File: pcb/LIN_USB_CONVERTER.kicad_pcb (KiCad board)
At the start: 2 copper layers, 17.8 x 34 mm, 32 parts, among them J1 Conn_01x03, J2 Conn_01x03, J3 GS2, J4 USB_A, J5 Conn_01x02, P2 CONN_01X05, U1 TJA1028, U2 MAX12931, U3 MCP1700T-3302E/TT, U4 STM32F042G4U6

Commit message: Kicad update
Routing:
- net -BATT: track 62.3 -> 62.7 mm, vias 2 -> 3
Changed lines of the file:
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@@
-(kicad_pcb (version 4) (host pcbnew 4.0.7)
+(kicad_pcb (version 20171130) (host pcbnew "(2018-02-16 revision c95340fba)-makepkg")
   (general
-    (links 84)
-    (no_connects 7)
-    (area 140.121999 78.203999 158.102001 112.440001)
     (thickness 1.6)
     (drawings 20)
-    (tracks 272)
+    (tracks 276)
     (zones 0)
     (modules 32)
@@
       (layerselection 0x3ffff_80000001)
       (usegerberextensions true)
+      (usegerberattributes false)
+      (usegerberadvancedattributes false)
+      (creategerberjobfile false)
       (excludeedgelayer true)
       (linewidth 0.100000)
@@
       (hpglpenspeed 20)
       (hpglpendiameter 15)
-      (hpglpenoverlay 2)
       (psnegative false)
       (psa4output false)
@@
     (tags "capacitor 0402")
     (attr smd)
-    (fp_text reference C8 (at 1.5 0 540) (layer F.SilkS)
+    (fp_text reference C8 (at 1.5 0 180) (layer F.SilkS)
       (effects (font (size 0.4 0.4) (thickness 0.09)))
     )
@@
     (tags "capacitor 0402")
     (attr smd)
-    (fp_text reference C3 (at 1.524 0 540) (layer F.SilkS)
+    (fp_text reference C3 (at 1.524 0 180) (layer F.SilkS)
       (effects (font (size 0.4 0.4) (thickness 0.09)))
     )
@@
     (tags "capacitor 0603")
     (attr smd)
-    (fp_text reference C2 (at 1.778 0 360) (layer F.SilkS)
+    (fp_text reference C2 (at 1.778 0) (layer F.SilkS)
       (effects (font (size 0.4 0.4) (thickness 0.09)))
     )
@@
     (tags "capacitor 0402")
     (attr smd)
-    (fp_text reference C6 (at -1.524 0 450) (layer F.SilkS)
+    (fp_text reference C6 (at -1.524 0 90) (layer F.SilkS)
       (effects (font (size 0.4 0.4) (thickness 0.09)))
     )
@@
     (descr "Through hole straight pin header, 1x03, 2.54mm pitch, single row")
     (tags "Through hole pin header THT 1x03 2.54mm single row")
-    (fp_text reference J1 (at 1.27 1.524 450) (layer B.SilkS)
+    (fp_text reference J1 (at 1.27 1.524 90) (layer B.SilkS)
       (effects (font (size 0.4 0.4) (thickness 0.09)) (justify mirror))
     )
@@
     (fp_line (start 1.8 -6.85) (end 1.8 1.8) (layer B.CrtYd) (width 0.05))
     (fp_line (start 1.8 1.8) (end -1.8 1.8) (layer B.CrtYd) (width 0.05))
-    (fp_text user %R (at 0 -2.54 540) (layer B.Fab)
+    (fp_text user %R (at 0 -2.54 180) (layer B.Fab)
       (effects (font (size 0.4 0.4) (thickness 0.09)) (justify mirror))
     )
@@
     (fp_line (start 1.8 -4.35) (end 1.8 1.8) (layer B.CrtYd) (width 0.05))
     (fp_line (start 1.8 1.8) (end -1.8 1.8) (layer B.CrtYd) (width 0.05))
-    (fp_text user %R (at 0 -1.27 450) (layer B.Fab)
+    (fp_text user %R (at 0 -1.27 90) (layer B.Fab)
       (effects (font (size 0.4 0.4) (thickness 0.09)) (justify mirror))
     )
@@
     (pad "" np_thru_hole circle (at 5.842 -2.413) (size 1.5 1.5) (drill 1.5) (layers *.Cu *.Mask))
     (model Connect.3dshapes/USB_A.wrl
-      (at (xyz 0.14 0 0))
+      (offset (xyz 3.555999946594238 0 0))
       (scale (xyz 1 1 1))
       (rotate (xyz 0 0 90))
@@
   (segment (start 156.462 86.324) (end 155.554 85.416) (width 0.25) (layer F.Cu) (net 8))
   (segment (start 155.554 85.416) (end 155.504 85.416) (width 0.25) (layer F.Cu) (net 8))
+  (segment (start 151.143002 95.83) (end 150.382 95.83) (width 0.25) (layer F.Cu) (net 9))
+  (segment (start 151.905002 96.592) (end 151.143002 95.83) (width 0.25) (layer F.Cu) (net 9))
+  (segment (start 150.382 95.83) (end 149.227978 96.984022) (width 0.25) (layer F.Cu) (net 9))
+  (segment (start 149.227978 96.984022) (end 149.227978 98.484022) (width 0.25) (layer F.Cu) (net 9))
+  (segment (start 149.227978 98.484022) (end 147.588 100.124) (width 0.25) (layer F.Cu) (net 9))
+  (segment (start 147.588 100.124) (end 147.588 100.87) (width 0.25) (layer F.Cu) (net 9))
+  (segment (start 151.905002 96.338998) (end 152.16 96.084) (width 0.25) (layer F.Cu) (net 9))
+  (via (at 152.16 96.084) (size 0.6) (drill 0.4) (layers F.Cu B.Cu) (net 9))
+  (segment (start 152.525002 97.212) (end 151.905002 96.592) (width 0.25) (layer F.Cu) (net 9))
+  (segment (start 151.905002 96.592) (end 151.905002 96.338998) (width 0.25) (layer F.Cu) (net 9))
   (segment (start 154.192 97.212) (end 153.56 97.212) (width 0.25) (layer F.Cu) (net 9))
-  (segment (start 147.588 100.124) (end 147.588 100.87) (width 0.25) (layer F.Cu) (net 9))
-  (segment (start 152.525002 97.212) (end 151.143002 95.83) (width 0.25) (layer F.Cu) (net 9))
-  (segment (start 149.227978 98.484022) (end 147.588 100.124) (width 0.25) (layer F.Cu) (net 9))
-  (segment (start 151.143002 95.83) (end 149.874 95.83) (width 0.25) (layer F.Cu) (net 9))
   (segment (start 154.192 97.212) (end 152.525002 97.212) (width 0.25) (layer F.Cu) (net 9))
-  (segment (start 149.874 95.83) (end 149.227978 96.476022) (width 0.25) (layer F.Cu) (net 9))
-  (segment (start 149.227978 96.476022) (end 149.227978 98.484022) (width 0.25) (layer F.Cu) (net 9))
   (segment (start 150.128 106.244) (end 150.128 109.292) (width 0.25) (layer F.Cu) (net 9))
   (segment (start 150.128 109.292) (end 150.382 109.546) (width 0.25) (layer F.Cu) (net 9))
@@
     (polygon
       (pts
-        (xy 140.222 97.1) (xy 149.366 97.1) (xy 149.366 94.306) (xy 154.192 94.306) (xy 154.192 91.258)
+        (xy 140.222 97.1) (xy 148.096 97.1) (xy 148.096 94.56) (xy 154.192 94.56) (xy 154.192 91.258)
         (xy 157.748 91.258) (xy 158.002 91.258) (xy 158.002 78.304) (xy 140.222 78.304)
       )
@@
     (polygon
       (pts
-        (xy 140.222 97.1) (xy 149.366 97.1) (xy 149.366 94.306) (xy 154.192 94.306) (xy 154.192 91.258)
+        (xy 140.222 97.1) (xy 148.096 97.1) (xy 148.096 94.56) (xy 154.192 94.56) (xy 154.192 91.258)
         (xy 157.748 91.258) (xy 158.002 91.258) (xy 158.002 78.304) (xy 140.222 78.304)
       )

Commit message: frame reception fixes
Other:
- board text removed: "+BAT"
- board text removed: "-BAT"
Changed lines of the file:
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@@
     (aux_axis_origin 154.7 109.8)
     (grid_origin 154.7 109.8)
-    (visible_elements 7FFEDF7F)
+    (visible_elements 7FFFDF7F)
     (pcbplotparams
       (layerselection 0x3ffff_80000001)
@@
     (effects (font (size 0.6 0.6) (thickness 0.1)) (justify mirror))
   )
-  (gr_text -BAT (at 153.43 99.64) (layer B.SilkS)
+  (gr_text BAT- (at 153.43 99.64) (layer B.SilkS)
     (effects (font (size 0.6 0.6) (thickness 0.1)) (justify mirror))
   )
-  (gr_text +BAT (at 150.89 99.64) (layer B.SilkS)
+  (gr_text BAT+ (at 150.89 99.64) (layer B.SilkS)
     (effects (font (size 0.6 0.6) (thickness 0.1)) (justify mirror))
   )
@@
   (gr_line (start 140.222 78.304) (end 158.002 78.304) (layer Edge.Cuts) (width 0.2))
   (gr_line (start 140.222 112.304) (end 140.222 78.304) (layer Edge.Cuts) (width 0.2))
-  (gr_text GND (at 141.746 85.162 180) (layer F.SilkS)
+  (gr_text GND (at 141.492 82.622 180) (layer F.SilkS)
     (effects (font (size 0.6 0.6) (thickness 0.1)))
   )
-  (gr_text RST (at 143.524 93.798 90) (layer F.SilkS)
+  (gr_text RST (at 141.492 92.782) (layer F.SilkS)
     (effects (font (size 0.6 0.6) (thickness 0.1)))
   )
-  (gr_text DIO (at 141.746 87.702 180) (layer F.SilkS)
+  (gr_text DIO (at 141.492 85.162 180) (layer F.SilkS)
     (effects (font (size 0.6 0.6) (thickness 0.1)))
   )
-  (gr_text 3V3 (at 141.746 90.242) (layer F.SilkS)
+  (gr_text CLK (at 141.492 87.702) (layer F.SilkS)
     (effects (font (size 0.6 0.6) (thickness 0.1)))
   )
-  (gr_text CLK (at 141.746 92.782) (layer F.SilkS)
+  (gr_text 3V3 (at 141.492 90.242) (layer F.SilkS)
     (effects (font (size 0.6 0.6) (thickness 0.1)))
   )

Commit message: Naming update
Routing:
- net GND: track 36.0 -> 38.7 mm, vias 3 -> 4
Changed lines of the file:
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@@
     (thickness 1.6)
     (drawings 20)
-    (tracks 276)
+    (tracks 280)
     (zones 0)
     (modules 32)
@@
   )
   (gr_line (start 155.867134 85.010166) (end 153.221534 85.010166) (angle 90) (layer B.SilkS) (width 0.2))
+  (segment (start 152.668 88.718) (end 152.16 88.718) (width 0.25) (layer F.Cu) (net 1))
+  (segment (start 153.618 87.768) (end 152.668 88.718) (width 0.25) (layer F.Cu) (net 1))
+  (via (at 152.16 88.718) (size 0.6) (drill 0.4) (layers F.Cu B.Cu) (net 1))
+  (segment (start 154.462 87.768) (end 153.618 87.768) (width 0.25) (layer F.Cu) (net 1))
   (segment (start 152.668 86.474) (end 152.168 86.474) (width 0.25) (layer F.Cu) (net 1))
   (segment (start 152.168 86.474) (end 150.983 85.289) (width 0.25) (layer F.Cu) (net 1))
@@
   (segment (start 141.746 94.052) (end 142.146 94.052) (width 0.25) (layer F.Cu) (net 7))
   (segment (start 148.482 89.864) (end 148.482 90.389) (width 0.25) (layer F.Cu) (net 7))
+  (segment (start 152.41486 82.87812) (end 153.165429 83.628689) (width 0.25) (layer F.Cu) (net 8))
   (segment (start 155.504 85.416) (end 155.504 84.916) (width 0.25) (layer F.Cu) (net 8))
   (segment (start 155.504 84.916) (end 154.216689 83.628689) (width 0.25) (layer F.Cu) (net 8))
   (segment (start 154.216689 83.628689) (end 153.165429 83.628689) (width 0.25) (layer F.Cu) (net 8))
-  (segment (start 153.165429 83.628689) (end 152.41486 82.87812) (width 0.25) (layer F.Cu) (net 8))
   (segment (start 156.462 88.718) (end 156.462 86.324) (width 0.25) (layer F.Cu) (net 8))
   (segment (start 156.462 86.324) (end 155.554 85.416) (width 0.25) (layer F.Cu) (net 8))

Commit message: PCB release
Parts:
- added C7: 10u, Capacitors_SMD:C_0402, F.Cu at (156.5, 98.4)
- J2: value Conn_01x03 -> TerminalBlock
- U1: value TJA1028 -> TJA1028TK/3V3/20/J
- U2: value MAX12931 -> MAX12931BASA+
- moved C3 0.28 mm to (155.2, 98.4)
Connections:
- U1 pad 7: Net-(U1-Pad7) -> (no net)
- U4 pad 10: Net-(U4-Pad10) -> (no net)
- U4 pad 11: Net-(U4-Pad11) -> (no net)
- U4 pad 12: Net-(U4-Pad12) -> (no net)
- U4 pad 13: Net-(U4-Pad13) -> (no net)
- U4 pad 2: Net-(U4-Pad2) -> (no net)
- U4 pad 23: Net-(U4-Pad23) -> (no net)
- U4 pad 24: Net-(U4-Pad24) -> (no net)
- U4 pad 25: Net-(U4-Pad25) -> (no net)
- U4 pad 26: Net-(U4-Pad26) -> (no net)
- U4 pad 3: Net-(U4-Pad3) -> (no net)
- U4 pad 6: Net-(U4-Pad6) -> (no net)
- U4 pad 9: Net-(U4-Pad9) -> (no net)
- mh1 pad 1: (no net) -> -BATT
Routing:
- net Net-(C1-Pad1): track 26.1 -> 28.3 mm
- net -BATT: track 62.7 -> 64.2 mm
- net +3.3VA: track 22.4 -> 23.7 mm
- net Net-(J3-Pad2): track 9.81 -> 10.5 mm
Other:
- board text added: "MASTER RESISTOR"

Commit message: PCB release
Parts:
- C7: footprint Capacitors_SMD:C_0402 -> Capacitors_SMD:C_0603
- moved C7 0.23 mm to (156.4, 98.6)
- moved C3 0.13 mm to (155.1, 98.4)
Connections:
- D1 pad 1: Net-(D1-Pad1) -> +BATT
- D1 pad 2: +BATT -> Net-(D1-Pad2)
- D3 pad 1: +BATT -> Net-(D3-Pad1)
- D3 pad 2: Net-(D3-Pad2) -> +BATT
- J1 pad 1: +BATT -> Net-(D1-Pad2)
- J2 pad 3: +BATT -> Net-(D1-Pad2)
- R1 pad 2: Net-(D3-Pad2) -> Net-(D3-Pad1)
- R2 pad 2: Net-(D1-Pad1) -> +BATT
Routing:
- net Net-(D1-Pad2): track 0.00 -> 18.4 mm
- net Net-(D3-Pad1): track 0.00 -> 4.56 mm
- net Net-(D1-Pad1): track 4.55 -> 0.00 mm
- net Net-(D3-Pad2): track 2.09 -> 0.00 mm
- net -BATT: track 64.2 -> 62.1 mm
- net +BATT: track 20.0 -> 18.3 mm

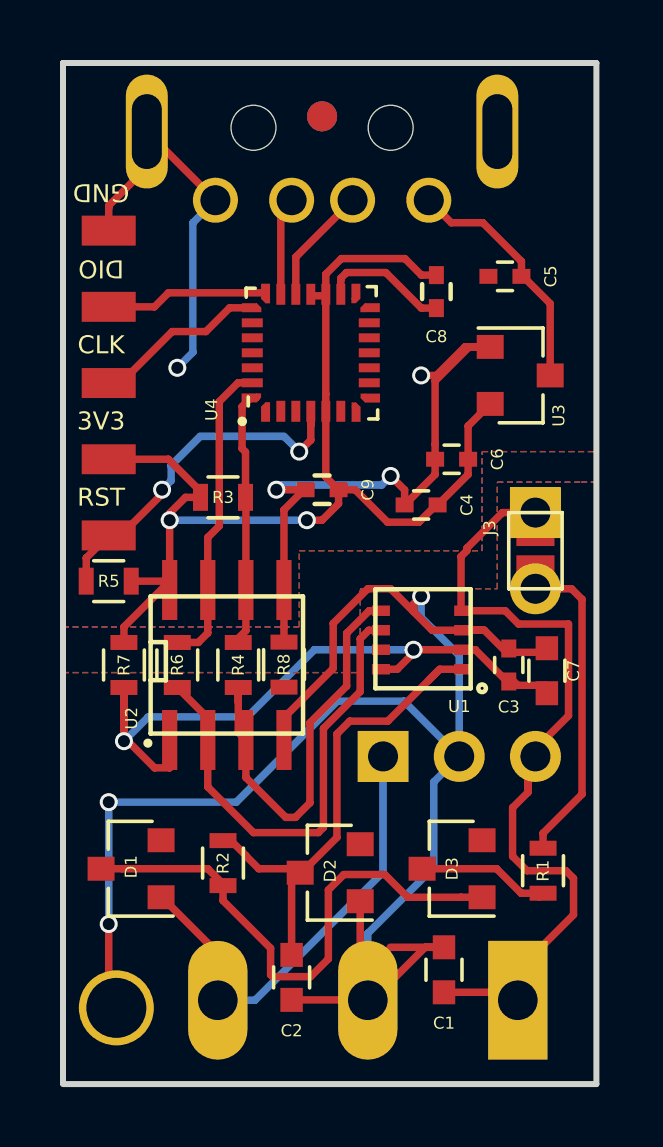
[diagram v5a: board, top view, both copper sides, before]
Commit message: Remove of galvanic spearator
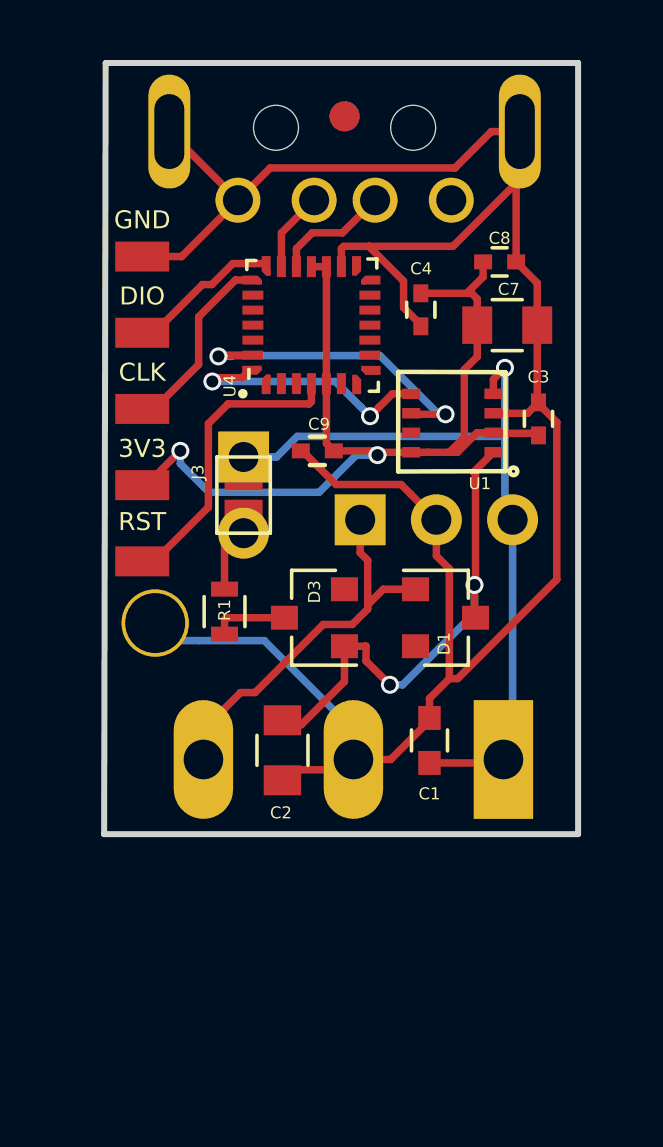
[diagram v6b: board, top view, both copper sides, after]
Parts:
- removed C5, C6: 100n, Capacitors_SMD:C_0402
- removed D2: 1N5819HW-7-F, Diodes_SMD:D_SOT-23_ANK
- removed R2: 50, Resistors_SMD:R_0603
- removed R3, R5: 10k, Resistors_SMD:R_0603
- removed R4, R6, R7, R8: 0, Resistors_SMD:R_0603
- removed U2: MAX12931BASA+, usb_ccb_custom:SOIC-8-N_MAXIM
- removed U3: MCP1700T-3302E/TT, TO_SOT_Packages_SMD:SOT-23
- C2: footprint Capacitors_SMD:C_0603 -> Capacitors_SMD:C_0805
- C7: value 10u -> 4,7u; footprint Capacitors_SMD:C_0603 -> Capacitors_SMD:C_0805
- U1: footprint usb_ccb_custom:HVSON8 -> ucan_custom:HVSON8
- moved R1 13.7 mm to (145.6, 96.6)
- moved D1 13.4 mm to (153.0, 96.8), turned to 0 degrees
- moved mh1 12.9 mm to (143.3, 97.0)
- moved C7 11.6 mm to (155.0, 87.0), turned to 180 degrees
- moved J3 9.90 mm to (146.2, 92.7)
- moved J5 9.90 mm to (146.2, 91.4)
- moved D3 9.54 mm to (148.6, 96.8)
- moved C3 8.26 mm to (156.1, 90.2)
- moved J2 8.04 mm to (154.9, 101.5)
- moved J1 7.92 mm to (150.1, 93.5)
- moved C1 7.66 mm to (152.4, 100.9)
- moved C2 7.58 mm to (147.5, 101.2)
- moved U1 7.30 mm to (151.9, 91.3)
- moved C4 6.51 mm to (152.1, 86.5), turned to 270 degrees
- moved C8 2.33 mm to (154.8, 84.9), turned to 0 degrees
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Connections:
- C2 pad 1: Net-(C2-Pad1) -> +BATT
- C4 pad 1: +3V3 -> +3.3VA
- C4 pad 2: GND -> -BATT
- C8 pad 1: +3V3 -> +3.3VA
- C8 pad 2: GND -> -BATT
- C9 pad 1: +3V3 -> +3.3VA
- C9 pad 2: GND -> -BATT
- J4 pad 1: +5V -> (no net)
- J4 pad 4: GND -> -BATT
- J4 pad 5: GND -> -BATT
- P2 pad 1: GND -> -BATT
- P2 pad 4: +3V3 -> +3.3VA
- U1 pad 1: Net-(C2-Pad1) -> +BATT
- U1 pad 5: Net-(R4-Pad1) -> USART_RX
- U1 pad 6: Net-(R6-Pad1) -> USART_TX
- U4 pad 16: GND -> -BATT
- U4 pad 17: +3V3 -> +3.3VA
- U4 pad 18: +3V3 -> +3.3VA
- U4 pad 27: /USART_TX -> USART_TX
- U4 pad 28: /USART_RX -> USART_RX
- U4 pad 5: +3V3 -> +3.3VA
- mh1 pad 1: -BATT -> (no net)
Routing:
- net GND: track 38.7 -> 0.00 mm, vias 4 -> 0
- net +3V3: track 38.2 -> 0.00 mm, vias 2 -> 0
- net -BATT: track 62.1 -> 79.3 mm, vias 3 -> 0
- net Net-(C2-Pad1): track 16.5 -> 0.00 mm
- net Net-(R6-Pad1): track 16.0 -> 0.00 mm
- net Net-(R4-Pad1): track 14.2 -> 0.00 mm
- net USART_TX: track 0.00 -> 10.7 mm, vias 0 -> 2
- net /USART_TX: track 10.7 -> 0.00 mm
- net USART_RX: track 0.00 -> 9.43 mm, vias 0 -> 2
- net +3.3VA: track 23.5 -> 32.3 mm
- net Net-(J3-Pad2): track 10.5 -> 1.95 mm
- net +5V: track 8.16 -> 0.00 mm
- net /USART_RX: track 7.96 -> 0.00 mm
- net Net-(D1-Pad2): track 18.4 -> 13.0 mm
- net Net-(P2-Pad5): track 12.2 -> 10.1 mm, vias 2 -> 0
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- removed copper zone on B.Cu, net GND
- removed copper zone on F.Cu, net GND
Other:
- board size 17.8 x 34 mm -> 15.8 x 25.7 mm
- board text added: "LUC1.1"
- board text added: "U1"
- board text removed: "LUC1.0"

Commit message: TJA package update
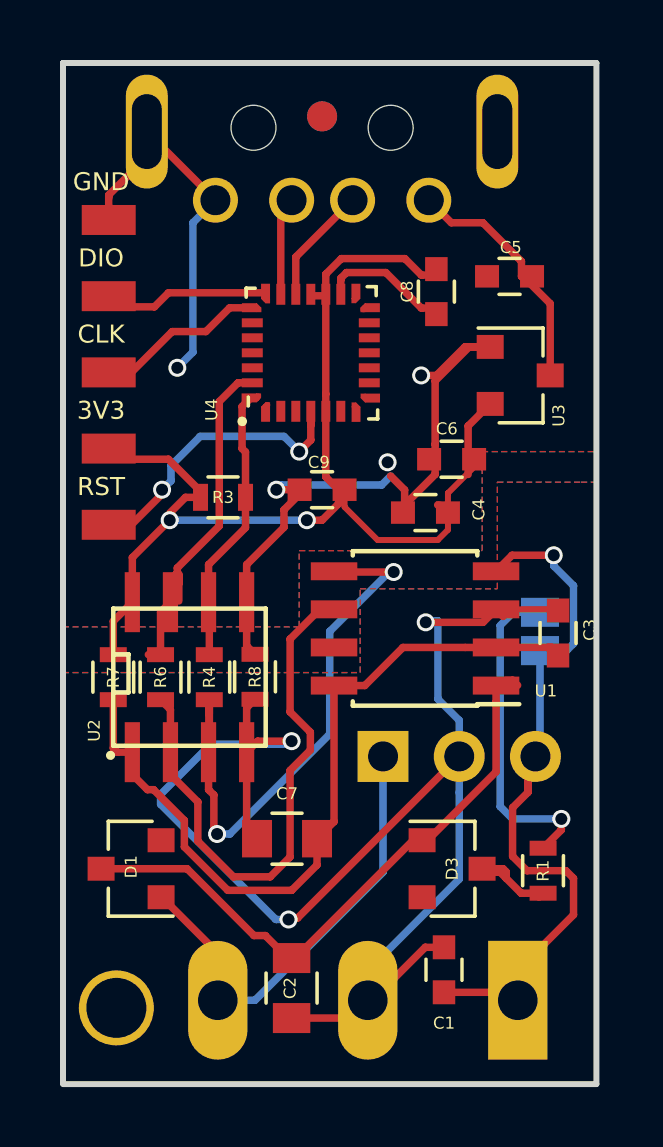
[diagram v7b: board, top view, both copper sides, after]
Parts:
- removed J5: Conn_01x02, Pin_Headers:Pin_Header_Straight_1x02_Pitch2.54mm
- added C5: 1u, Capacitors_SMD:C_0603, F.Cu at (155.1, 85.4)
- added C6: 1u, Capacitors_SMD:C_0603, F.Cu at (153.2, 91.5)
- added R3: 10k, Resistors_SMD:R_0603, F.Cu at (145.6, 92.8)
- added R4: 0, Resistors_SMD:R_0603, F.Cu at (145.1, 98.8)
- added R6: 0, Resistors_SMD:R_0603, F.Cu at (143.5, 98.8)
- added R7: 0, Resistors_SMD:R_0603, F.Cu at (141.9, 98.8)
- added R8: 0, Resistors_SMD:R_0603, F.Cu at (146.6, 98.8)
- added U2: MAX12931BASA+, usb_ccb_custom:SOIC-8-N_MAXIM, F.Cu at (144.4, 98.8)
- added U3: MCP1700T-3302E/TT, TO_SOT_Packages_SMD:SOT-23, F.Cu at (155.5, 88.7)
- C3, C4, C8, C9: footprint Capacitors_SMD:C_0402 -> Capacitors_SMD:C_0603
- C7: value 4,7u -> 10u
- J3: moved to B.Cu
- U1: footprint ucan_custom:HVSON8 -> Housings_SOIC:SOIC-8_3.9x4.9mm_Pitch1.27mm
- moved C7 18.6 mm to (147.7, 104.2), turned to 0 degrees
- moved R1 13.7 mm to (156.2, 105.2)
- moved D1 13.4 mm to (142.5, 105.2), turned to 180 degrees
- moved mh1 12.9 mm to (142.0, 109.8)
- moved J3 10.9 mm to (156.1, 97.3)
- moved D3 9.54 mm to (153.2, 105.2), turned to 0 degrees
- moved J2 8.04 mm to (155.4, 109.5)
- moved C2 7.93 mm to (147.8, 109.1)
- moved J1 7.92 mm to (150.9, 101.4)
- moved C1 7.66 mm to (152.9, 108.5)
- moved C3 7.17 mm to (156.7, 97.3)
- moved C4 6.76 mm to (152.3, 93.3), turned to 180 degrees
- moved U1 5.87 mm to (152.0, 97.2), turned to 180 degrees
- moved C8 2.33 mm to (152.7, 85.9), turned to 270 degrees
- moved P2 1.65 mm to (141.7, 87.3)
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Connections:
- C4 pad 1: +3.3VA -> +3V3
- C4 pad 2: -BATT -> GND
- C8 pad 1: +3.3VA -> +3V3
- C8 pad 2: -BATT -> GND
- C9 pad 1: +3.3VA -> +3V3
- C9 pad 2: -BATT -> GND
- J4 pad 1: (no net) -> +5V
- J4 pad 4: -BATT -> GND
- J4 pad 5: -BATT -> GND
- P2 pad 1: -BATT -> GND
- P2 pad 4: +3.3VA -> +3V3
- U1 pad 5: USART_RX -> Net-(R4-Pad1)
- U1 pad 6: USART_TX -> Net-(R6-Pad1)
- U4 pad 16: -BATT -> GND
- U4 pad 17: +3.3VA -> +3V3
- U4 pad 18: +3.3VA -> +3V3
- U4 pad 27: USART_TX -> /USART_TX
- U4 pad 28: USART_RX -> /USART_RX
- U4 pad 5: +3.3VA -> +3V3
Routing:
- net +3V3: track 0.00 -> 40.2 mm, vias 0 -> 2
- net GND: track 0.00 -> 39.7 mm, vias 0 -> 4
- net -BATT: track 79.3 -> 52.3 mm, vias 0 -> 3
- net Net-(R4-Pad1): track 0.00 -> 20.1 mm, vias 0 -> 2
- net Net-(R6-Pad1): track 0.00 -> 18.8 mm
- net /USART_TX: track 0.00 -> 12.6 mm
- net USART_TX: track 10.7 -> 0.00 mm, vias 2 -> 0
- net /USART_RX: track 0.00 -> 10.2 mm
- net USART_RX: track 9.43 -> 0.00 mm, vias 2 -> 0
- net Net-(J3-Pad2): track 1.95 -> 11.0 mm, vias 0 -> 1
- net +5V: track 0.00 -> 8.16 mm
- net Net-(D1-Pad2): track 13.0 -> 18.4 mm
- net +3.3VA: track 32.3 -> 27.9 mm, vias 2 -> 0
- net +BATT: track 16.8 -> 20.3 mm, vias 2 -> 0
- net Net-(C1-Pad1): track 26.3 -> 24.8 mm
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- added copper zone on B.Cu, net GND
- added copper zone on F.Cu, net GND
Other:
- board size 15.8 x 25.7 mm -> 17.8 x 34 mm
- board text added: "LUC1.0"
- board text removed: "BAT-"
- board text removed: "LUC1.1"
- board text removed: "U1"
